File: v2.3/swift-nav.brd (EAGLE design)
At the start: 53 x 53 mm, 151 parts, among them J1 SMA_EDGE, J6 ZX62-B-5PA, Q1 IRLML6401, U1 6SLX9FTG256, U10 MAX2769, U12 PT7M8206B33TA5EX, U13 M25PX80, U2 LTC3407A_DFN, U3 STM32-M-64-LQFP, U4 7Q-16.368MBG-T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

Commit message: Gettin' urr dunn
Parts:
- moved R1 3.33 mm to (32.1, 16.5)
- moved JP8 2.34 mm to (46.3, 5.99)
- moved JP10 1.35 mm to (13.6, 5.96)
- moved JP9 0.42 mm to (6.16, 45.3)
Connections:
- removed net N$1: X3.12
- net DEBUG0: now also U1.R1; no longer U1.L1
- net DEBUG1: now also U1.N1; no longer U1.J1
- net DEBUG2: now also U1.M1; no longer U1.G1
- net DEBUG3: now also U1.L1; no longer U1.F1
- net DEBUG4: now also U1.J1; no longer U1.D1
- net DEBUG5: now also U1.H3; no longer U1.C1
- net DEBUG6: now also U1.F1; no longer U1.B1
- net DEBUG7: now also U1.E1
- net DEBUG8: now also U1.D1
- net DEBUG9: now also U1.C1
- net V+: now also X3.12
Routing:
- net GND: track 75.1 -> 109.8 mm, vias 401 -> 311
- net N$39: track 60.2 -> 87.1 mm, vias 4 -> 3
- net VCCIO: track 140.4 -> 165.0 mm, vias 75 -> 79
- net N$59: track 53.4 -> 77.7 mm, vias 4 -> 3
- net V+: track 128.8 -> 143.2 mm, vias 9 -> 10
- net DEBUG9: track 0.00 -> 8.13 mm, vias 0 -> 2
- net DEBUG8: track 0.00 -> 8.11 mm, vias 0 -> 2
- net DEBUG7: track 0.00 -> 7.79 mm, vias 0 -> 2
- net N$55: track 28.2 -> 31.4 mm
- net N$24: track 21.9 -> 25.0 mm
- net VCCINT: track 72.6 -> 75.1 mm
- net N$16: track 8.33 -> 5.82 mm
- net DEBUG5: track 8.25 -> 10.0 mm
- net VDD: track 43.0 -> 44.7 mm
- net FTDI_NRST: track 102.7 -> 104.3 mm
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
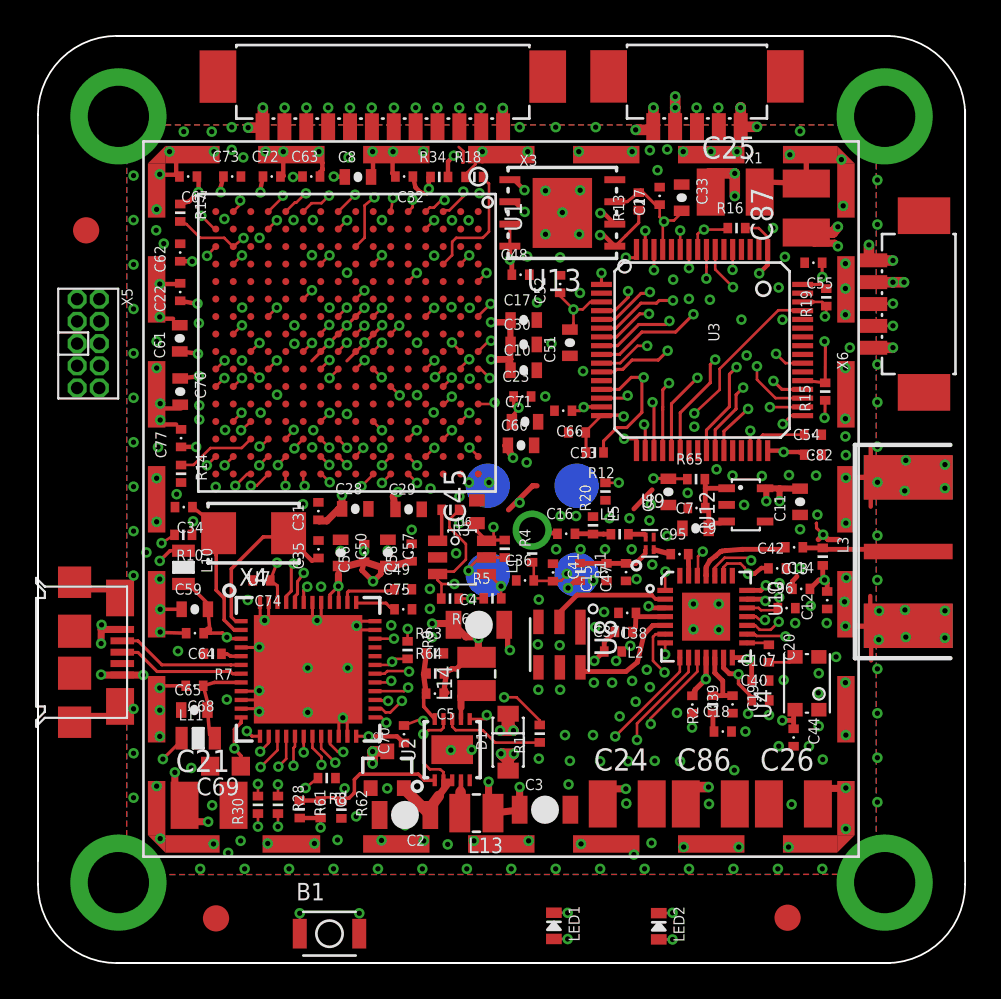
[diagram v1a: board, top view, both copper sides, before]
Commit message: Moving around some vias to reduce large gaps in ground plane
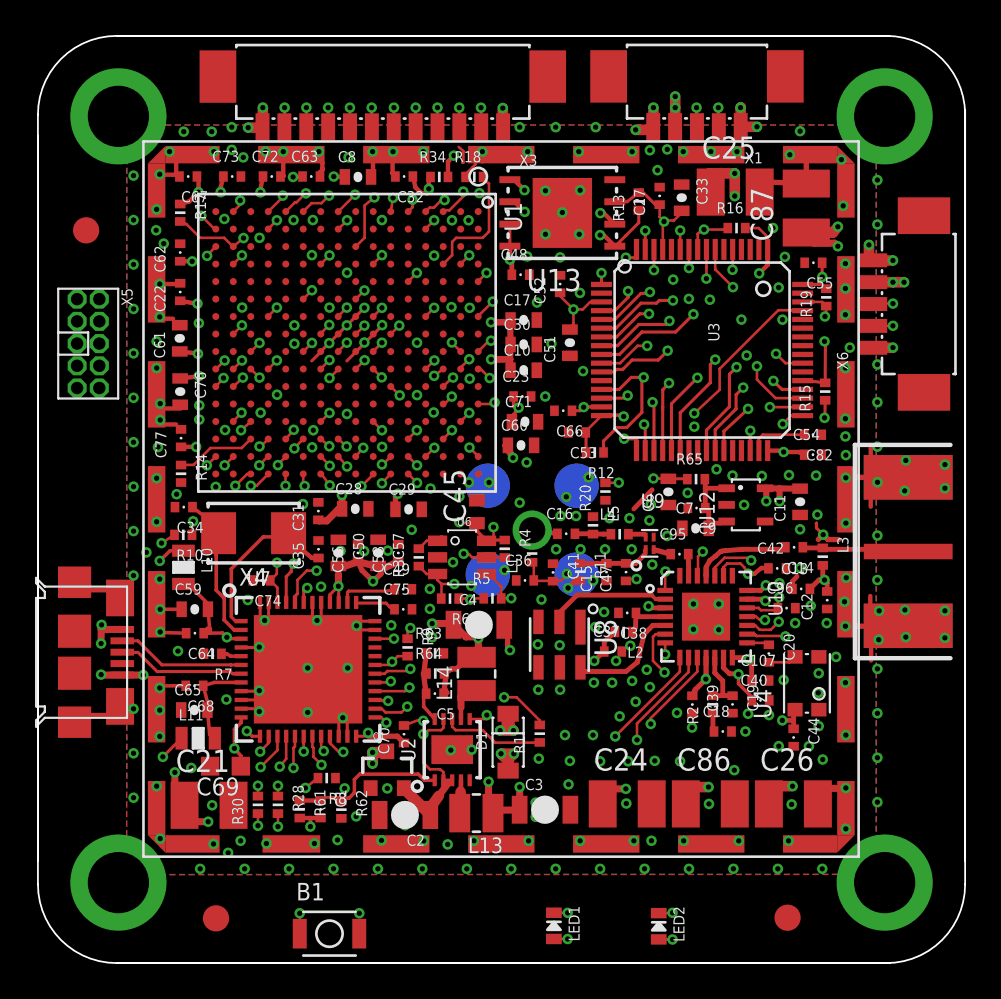
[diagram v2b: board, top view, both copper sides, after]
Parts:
- moved R3 3.27 mm to (25.2, 26.6), turned to 90 degrees
- moved C58 0.76 mm to (24.0, 26.8)
- moved C57 0.56 mm to (22.8, 26.9)
- moved C56 0.36 mm to (21.7, 26.8)
- moved R9 0.15 mm to (24.5, 21.4)
- moved C50 0.13 mm to (20.6, 26.8)
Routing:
- net V+: track 143.2 -> 128.3 mm, vias 10 -> 12
- net N$27: track 18.7 -> 13.9 mm
- net N$25: track 16.4 -> 19.2 mm
- net VCCIO: track 165.0 -> 166.7 mm, vias 79 -> 80
- net GND: track 109.8 -> 108.3 mm, vias 311 -> 315
- net JTAG_TCK: track 50.3 -> 49.1 mm
- net JTAG_TMS: track 51.7 -> 50.7 mm
- net FTDI_NRST: track 104.3 -> 104.9 mm
- net N$39: track 87.1 -> 87.7 mm
- net JTAG_RST: track 116.6 -> 117.2 mm

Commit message: Finished moving stuff around, routing, and DRC. Need to look at soldermask.
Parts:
- added C43, C46, C80, C81: 0.47uF, pel_dipol_comp:0402-CAP
- added C78: 4.7uF, pel_dipol_comp:0603-CAP
- moved R28 28.5 mm to (45.5, 15.0)
- moved R30 28.5 mm to (44.3, 15.0)
- moved R20 5.37 mm to (41.1, 31.6), turned to 0 degrees
- moved R4 3.90 mm to (26.9, 29.4), turned to 180 degrees
- moved C29 1.64 mm to (23.0, 29.0), turned to 270 degrees
- moved C17 1.48 mm to (31.0, 41.6)
- moved C68 1.04 mm to (13.4, 19.3)
- moved C28 0.98 mm to (20.7, 29.0), turned to 270 degrees
- moved C10 0.71 mm to (31.0, 38.0)
- moved C6 0.64 mm to (39.2, 29.8)
- moved R65 0.61 mm to (41.0, 30.5)
- moved C30 0.56 mm to (31.0, 39.3)
- moved C56 0.51 mm to (21.7, 26.3)
- moved C57 0.51 mm to (22.8, 26.3)
- moved C58 0.51 mm to (24.0, 26.3)
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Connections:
- net GND: now also C43.P$2, C46.P$2, C78.P$2, C80.P$2, C81.P$2
- net VCCINT: now also C43.P$1, C46.P$1, C78.P$1, C80.P$1, C81.P$1
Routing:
- net VCCINT: track 74.9 -> 49.5 mm, vias 15 -> 16
- net N$55: track 31.2 -> 16.3 mm
- net GND: track 108.3 -> 121.9 mm, vias 315 -> 337
- net JTAG_RST: track 117.2 -> 107.7 mm
- net VDD: track 44.9 -> 54.0 mm, vias 4 -> 6
- net MAX_PGM: track 31.3 -> 23.9 mm, vias 4 -> 2
- net VCCIO: track 166.7 -> 173.8 mm, vias 80 -> 79
- net N$24: track 24.9 -> 18.4 mm
- net FTDI_NRST: track 104.9 -> 100.9 mm
- net FPGA_DONE: track 51.6 -> 49.5 mm
- net N$23: track 15.0 -> 17.1 mm
- net N$18: track 68.5 -> 66.6 mm
- net FTDI_NOE: track 21.2 -> 19.8 mm
- net N$21: track 5.58 -> 4.15 mm
- net N$39: track 87.7 -> 86.5 mm
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- added copper zone on layer 15, net VCCINT

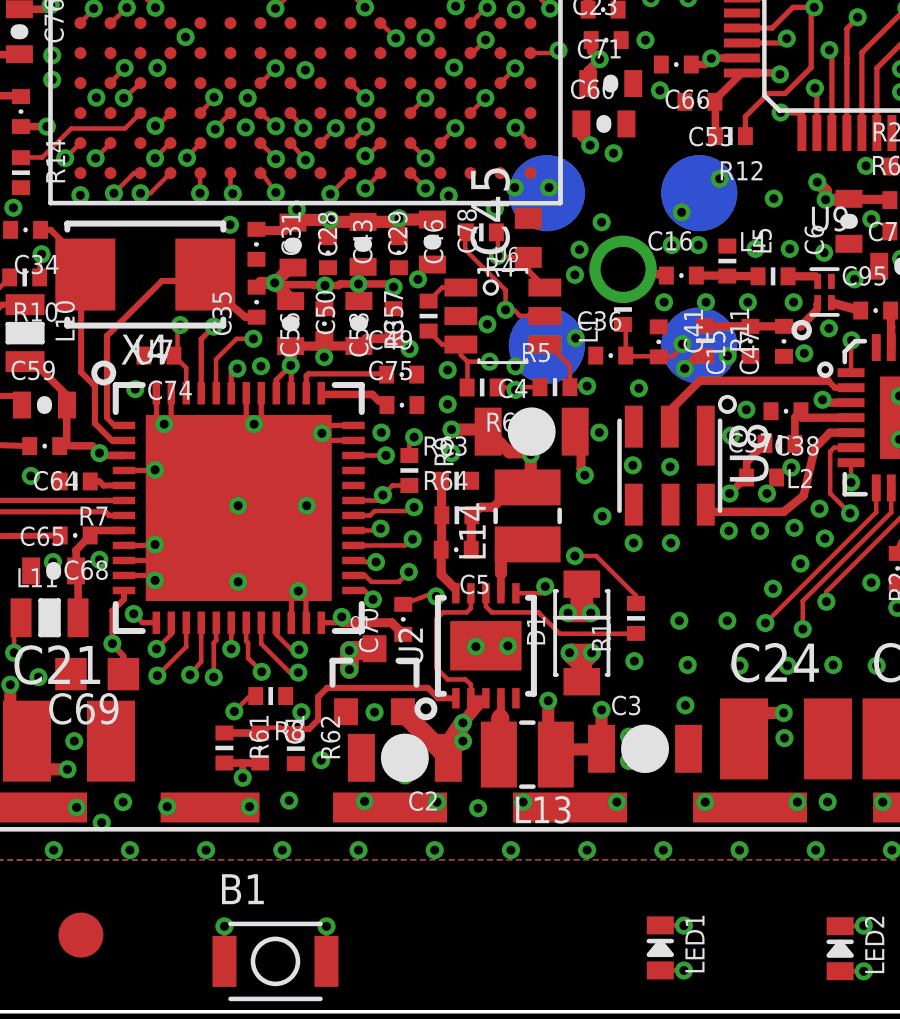
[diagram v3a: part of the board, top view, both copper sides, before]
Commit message: Couple part moves for spacing / solder mask clearance
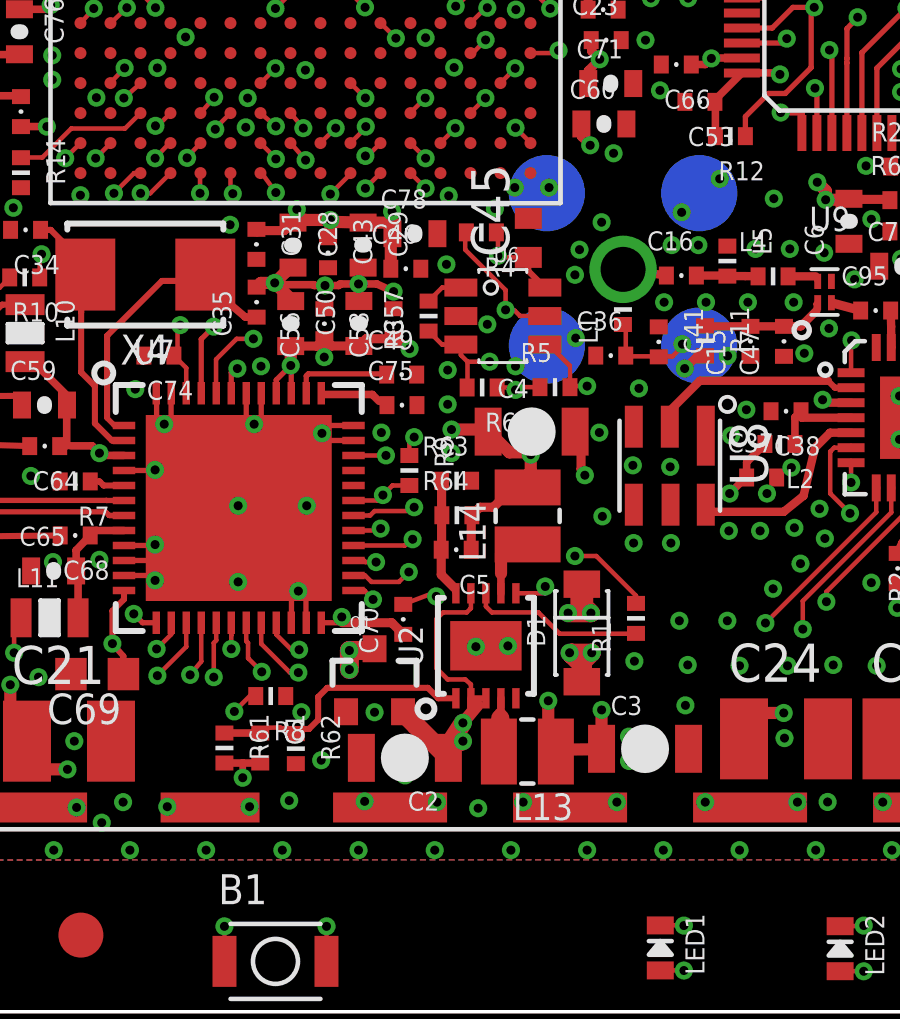
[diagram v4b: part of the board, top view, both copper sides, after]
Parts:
- moved C78 0.65 mm to (24.7, 29.3), turned to 0 degrees
- moved C46 0.58 mm to (24.4, 28.2), turned to 0 degrees
- moved L13 0.10 mm to (28.5, 12.1)

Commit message: Silkscreen and logo updated for v2.3
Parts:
- added U$2: LOGOLOGO3_SMALL, swift-nav:LOGO3_SMALL
- moved U$1 19.1 mm to (23.7, 24.3)
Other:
- board text added: "."
- board text added: "9"
- board text added: "Piksi"
- board text added: "UARTA"
- board text added: "UARTB"
- board text added: "v2.3.0"
- board text removed: "1"
- board text removed: "2"
- board text removed: "3"
- board text removed: "4"
- board text removed: "5"
- board text removed: "6"
- board text removed: "UART1"
- board text removed: "UART2"
- board text removed: "v2.2"

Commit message: v2.3 as sent out for production
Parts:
- moved J1 0.10 mm to (55.6, 26.9)
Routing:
- net GND: track 122.0 -> 153.6 mm
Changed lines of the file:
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@@
 <setting verticaltext="up"/>
 </settings>
-<grid distance="0.3" unitdist="mil" unit="mil" style="lines" multiple="1" display="yes" altdistance="0.25" altunitdist="mil" altunit="mil"/>
+<grid distance="1" unitdist="mil" unit="mil" style="lines" multiple="1" display="yes" altdistance="0.25" altunitdist="mil" altunit="mil"/>
 <layers>
 <layer number="1" name="Top" color="4" fill="1" visible="no" active="yes"/>
@@
 <layer number="14" name="Route14" color="1" fill="6" visible="no" active="yes"/>
 <layer number="15" name="Route15" color="4" fill="6" visible="no" active="yes"/>
-<layer number="16" name="Bottom" color="1" fill="1" visible="no" active="yes"/>
+<layer number="16" name="Bottom" color="1" fill="1" visible="yes" active="yes"/>
 <layer number="17" name="Pads" color="2" fill="1" visible="yes" active="yes"/>
-<layer number="18" name="Vias" color="2" fill="1" visible="no" active="yes"/>
-<layer number="19" name="Unrouted" color="6" fill="1" visible="no" active="yes"/>
+<layer number="18" name="Vias" color="2" fill="1" visible="yes" active="yes"/>
+<layer number="19" name="Unrouted" color="6" fill="1" visible="yes" active="yes"/>
 <layer number="20" name="Dimension" color="15" fill="1" visible="yes" active="yes"/>
 <layer number="21" name="tPlace" color="7" fill="1" visible="no" active="yes"/>
-<layer number="22" name="bPlace" color="7" fill="1" visible="no" active="yes"/>
+<layer number="22" name="bPlace" color="7" fill="1" visible="yes" active="yes"/>
 <layer number="23" name="tOrigins" color="15" fill="1" visible="no" active="yes"/>
-<layer number="24" name="bOrigins" color="15" fill="1" visible="no" active="yes"/>
+<layer number="24" name="bOrigins" color="15" fill="1" visible="yes" active="yes"/>
 <layer number="25" name="tNames" color="7" fill="1" visible="no" active="yes"/>
 <layer number="26" name="bNames" color="7" fill="1" visible="no" active="yes"/>
@@
 <layer number="28" name="bValues" color="7" fill="1" visible="no" active="yes"/>
 <layer number="29" name="tStop" color="7" fill="3" visible="no" active="yes"/>
-<layer number="30" name="bStop" color="7" fill="6" visible="no" active="yes"/>
+<layer number="30" name="bStop" color="7" fill="6" visible="yes" active="yes"/>
 <layer number="31" name="tCream" color="7" fill="4" visible="no" active="yes"/>
 <layer number="32" name="bCream" color="7" fill="5" visible="no" active="yes"/>
@@
 <param name="mdViaViaSameLayer" value="8mil"/>
 <param name="mnLayersViaInSmd" value="2"/>
-<param name="mdCopperDimension" value="25mil"/>
+<param name="mdCopperDimension" value="30mil"/>
 <param name="mdDrill" value="8mil"/>
 <param name="mdSmdStop" value="0mil"/>
@@
 <element name="B1" library="jobygnss" package="B3U-1000P" value="B3U-1000P" x="20.066" y="5.08"/>
 <element name="U5" library="joby_robotics" package="SMA_PATCH_SMDGND" value="SMA_PATCH_SMDGND" x="29.9" y="29.9" rot="MR270"/>
-<element name="J1" library="swift-nav" package="SMA_EDGE" value="SMA_EDGE" x="55.686959375" y="26.924" smashed="yes" rot="R270"/>
+<element name="J1" library="swift-nav" package="SMA_EDGE" value="SMA_EDGE" x="55.585359375" y="26.924" smashed="yes" rot="R270"/>
 <element name="C2" library="pel_dipol_comp" package="1206-CAP" value="10uF" x="24.3796" y="11.8646" rot="R180"/>
 <element name="C3" library="pel_dipol_comp" package="1206-CAP" value="10uF" x="32.385" y="12.1666"/>
@@
 <wire x1="7.0104" y1="19.8882" x2="8.8392" y2="19.8882" width="0.4064" layer="14"/>
 <via x="25.7654" y="28.3139" extent="1-16" drill="0.3"/>
-<wire x1="49.3268" y1="49.3268" x2="51.8" y2="51.8" width="0" layer="19" extent="1-1"/>
-<wire x1="53.009" y1="22.0354" x2="53.146959375" y2="22.6822" width="0" layer="19" extent="16-16"/>
-<wire x1="52.945" y1="30.3944" x2="53.146959375" y2="31.1658" width="0" layer="19" extent="16-16"/>
-<wire x1="52.959" y1="23.5854" x2="53.146959375" y2="22.6822" width="0" layer="19" extent="16-16"/>
-<wire x1="53.009" y1="32.1334" x2="53.146959375" y2="31.1658" width="0" layer="19" extent="16-16"/>
-<wire x1="55.245" y1="30.5444" x2="53.146959375" y2="31.1658" width="0" layer="19" extent="16-16"/>
-<wire x1="55.245" y1="31.8944" x2="55.245" y2="30.5444" width="0" layer="19" extent="1-1"/>
-<wire x1="55.245" y1="21.9894" x2="53.146959375" y2="22.6822" width="0" layer="19" extent="16-16"/>
-<wire x1="55.245" y1="23.5394" x2="55.245" y2="21.9894" width="0" layer="19" extent="1-1"/>
-<wire x1="8" y1="8" x2="10.3886" y2="10.5156" width="0" layer="19" extent="1-1"/>
-<wire x1="8" y1="51.8" x2="8.8646" y2="48.4124" width="0" layer="19" extent="1-1"/>
-<wire x1="51.8" y1="8" x2="48.2346" y2="8.7884" width="0" layer="19" extent="1-1"/>
+<wire x1="48.2346" y1="8.7884" x2="51.8" y2="8.7884" width="0.4064" layer="1"/>
+<wire x1="51.8" y1="8.7884" x2="51.8" y2="8" width="0.4064" layer="1"/>
+<wire x1="8" y1="8" x2="8.79348125" y2="8" width="0.4064" layer="1"/>
+<wire x1="8.79348125" y1="8" x2="8.79348125" y2="8.900159375" width="0.4064" layer="1"/>
+<wire x1="8.79348125" y1="8.900159375" x2="8.8646" y2="8.900159375" width="0.4064" layer="1"/>
+<wire x1="8.8646" y1="8.900159375" x2="8.8646" y2="12.8524" width="0.4064" layer="1"/>
+<wire x1="8" y1="51.8" x2="8.8646" y2="51.8" width="0.4064" layer="1"/>
+<wire x1="8.8646" y1="51.8" x2="8.8646" y2="48.4124" width="0.4064" layer="1"/>
+<wire x1="51.8" y1="51.8" x2="50.6349" y2="51.8" width="0.4064" layer="1"/>
+<wire x1="50.6349" y1="51.8" x2="50.6349" y2="50.97018125" width="0.4064" layer="1"/>
+<wire x1="50.6349" y1="50.97018125" x2="46.9646" y2="50.97018125" width="0.4064" layer="1"/>
+<wire x1="46.9646" y1="50.97018125" x2="46.9646" y2="50.9524" width="0.4064" layer="1"/>
+<wire x1="52.959" y1="23.5854" x2="53.009" y2="23.5854" width="0.4064" layer="1"/>
+<wire x1="53.009" y1="23.5854" x2="53.009" y2="22.0354" width="0.4064" layer="1"/>
+<wire x1="53.009" y1="22.0354" x2="55.245" y2="22.0354" width="0.4064" layer="1"/>
+<wire x1="55.245" y1="22.0354" x2="55.245" y2="21.9894" width="0.4064" layer="1"/>
+<wire x1="55.245" y1="22.0354" x2="55.245" y2="23.5394" width="0.4064" layer="1"/>
+<wire x1="53.009" y1="22.0354" x2="53.146959375" y2="22.0354" width="0.4064" layer="1"/>
+<wire x1="53.146959375" y1="22.0354" x2="53.045359375" y2="22.6822" width="0.4064" layer="1"/>
+<wire x1="55.245" y1="31.8944" x2="55.245" y2="30.5444" width="0.4064" layer="1"/>
+<wire x1="55.245" y1="30.5444" x2="53.146959375" y2="30.5444" width="0.4064" layer="1"/>
+<wire x1="52.945" y1="30.5444" x2="52.945" y2="30.3944" width="0.4064" layer="1"/>
+<wire x1="52.945" y1="30.5444" x2="53.146959375" y2="30.5444" width="0.4064" layer="1"/>
+<wire x1="53.146959375" y1="30.5444" x2="53.045359375" y2="31.1658" width="0.4064" layer="1"/>
+<wire x1="53.045359375" y1="31.1658" x2="53.009" y2="31.1658" width="0.4064" layer="1"/>
+<wire x1="53.009" y1="31.1658" x2="53.009" y2="32.1334" width="0.4064" layer="1"/>
 </signal>
 <signal name="N$3">
@@
 <wire x1="47.196759375" y1="27.08514375" x2="47.122959375" y2="27.167675" width="0.2286" layer="1"/>
 <contactref element="L3" pad="P$1"/>
-<wire x1="53.146959375" y1="26.924" x2="50.8762" y2="26.924" width="0.2794" layer="1"/>
+<wire x1="53.045359375" y1="26.924" x2="50.8762" y2="26.924" width="0.2794" layer="1"/>
 <wire x1="50.8762" y1="26.924" x2="50.7492" y2="27.051" width="0.2794" layer="1"/>
 <wire x1="50.7492" y1="27.051" x2="48.3409" y2="27.051" width="0.2794" layer="1"/>
